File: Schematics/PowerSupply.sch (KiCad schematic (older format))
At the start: 0 parts

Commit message: Updated schematics
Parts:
- added C33: 10u, Capacitors_SMD:C_0603, symbol C
- added C34: 10n, Capacitors_SMD:C_0402, symbol C
- added C35: 1u, Capacitors_SMD:C_0402, symbol C
- added C36: 100n, Capacitors_SMD:C_0402, symbol C
- added C37: 10p, Capacitors_SMD:C_0402, symbol C
- added C38, C39: 47n, Capacitors_SMD:C_0603, symbol C
- added D1: LED, LEDs:LED-1206, symbol LED
- added L1: 3.2u, symbol INDUCTOR
- added R31: 220R, Resistors_SMD:R_0603, symbol R
- added R32: 41.2k, Resistors_SMD:R_0402, symbol R
- added R33: 2.4M, Resistors_SMD:R_0402, symbol R
- added R34: 1M, Resistors_SMD:R_0402, symbol R
- added U13: LT8612, rgb:28QFN, symbol LT8612
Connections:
- net labels added: BST, FB, GND, IntVcc, PG, Rt, SS, SW, Vin, Vsupply
- wire segments 0 -> 47

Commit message: Removed RF. Placed all LED drivers and passives and begun routing
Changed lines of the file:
@@
 $Descr A4 11693 8268
 encoding utf-8
-Sheet 17 16
+Sheet 16 16
 Title ""
 Date ""
@@
 	3600 2900 3600 3800
 $Comp
-L GND #PWR0134
+L GND #PWR0117
 U 1 1 54BACD64
 P 3900 3900
-F 0 "#PWR0134" H 3900 3650 60  0001 C CNN
+F 0 "#PWR0117" H 3900 3650 60  0001 C CNN
 F 1 "GND" H 3900 3750 60  0000 C CNN
 F 2 "" H 3900 3900 60  0000 C CNN
@@
 	6050 3150 6050 3400
 Wire Wire Line
-	6950 3400 6050 3400
+	6050 3400 6950 3400
 Wire Wire Line
 	6950 3300 6950 3450
@@
 Connection ~ 7600 2750
 $Comp
-L GND #PWR0135
+L GND #PWR0118
 U 1 1 54BAE2C1
 P 4850 3900
-F 0 "#PWR0135" H 4850 3650 60  0001 C CNN
+F 0 "#PWR0118" H 4850 3650 60  0001 C CNN
 F 1 "GND" H 4850 3750 60  0000 C CNN
 F 2 "" H 4850 3900 60  0000 C CNN
@@
 $EndComp
 $Comp
-L GND #PWR0136
+L GND #PWR0119
 U 1 1 54BAE2D9
 P 5150 3900
-F 0 "#PWR0136" H 5150 3650 60  0001 C CNN
+F 0 "#PWR0119" H 5150 3650 60  0001 C CNN
 F 1 "GND" H 5150 3750 60  0000 C CNN
 F 2 "" H 5150 3900 60  0000 C CNN
@@
 $EndComp
 $Comp
-L GND #PWR0137
+L GND #PWR0120
 U 1 1 54BAE2F1
 P 6950 4000
-F 0 "#PWR0137" H 6950 3750 60  0001 C CNN
+F 0 "#PWR0120" H 6950 3750 60  0001 C CNN
 F 1 "GND" H 6950 3850 60  0000 C CNN
 F 2 "" H 6950 4000 60  0000 C CNN
@@
 $EndComp
 $Comp
-L GND #PWR0138
+L GND #PWR0121
 U 1 1 54BAE309
 P 7800 4050
-F 0 "#PWR0138" H 7800 3800 60  0001 C CNN
+F 0 "#PWR0121" H 7800 3800 60  0001 C CNN
 F 1 "GND" H 7800 3900 60  0000 C CNN
 F 2 "" H 7800 4050 60  0000 C CNN

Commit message: Changed lots
Finalised the Inductor. Closes #5
Changed USB Connector. Closes #4
Added four switches for a simple interface. Closes #7
Added a power jack. Closes #3
Found RTC Oscillator. Closes #1.
Added part numbers to all major components. Closes #2
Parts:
- L1: footprint (none) -> rgb:SD43; Part (none) -> SD43-332ML
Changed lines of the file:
@@
 F 0 "L1" V 6450 2500 50  0000 C CNN
 F 1 "3.2u" V 6450 2850 50  0000 C CNN
-F 2 "" H 6500 2750 60  0001 C CNN
-F 3 "" H 6500 2750 60  0000 C CNN
+F 2 "rgb:SD43" H 6500 2750 60  0001 C CNN
+F 3 "http://www.coilcraft.com/pdfs/sd43.pdf" H 6500 2750 60  0001 C CNN
+F 4 "SD43-332ML" V 6500 2750 60  0001 C CNN "Part"
 	1    6500 2750
 	0    -1   -1   0
@@
 	3600 2900 3600 3800
 $Comp
-L GND #PWR118
+L GND #PWR0119
 U 1 1 54BACD64
 P 3900 3900
-F 0 "#PWR118" H 3900 3650 60  0001 C CNN
+F 0 "#PWR0119" H 3900 3650 60  0001 C CNN
 F 1 "GND" H 3900 3750 60  0000 C CNN
 F 2 "" H 3900 3900 60  0000 C CNN
@@
 Connection ~ 7600 2750
 $Comp
-L GND #PWR119
+L GND #PWR0120
 U 1 1 54BAE2C1
 P 4850 3900
-F 0 "#PWR119" H 4850 3650 60  0001 C CNN
+F 0 "#PWR0120" H 4850 3650 60  0001 C CNN
 F 1 "GND" H 4850 3750 60  0000 C CNN
 F 2 "" H 4850 3900 60  0000 C CNN
@@
 $EndComp
 $Comp
-L GND #PWR120
+L GND #PWR0121
 U 1 1 54BAE2D9
 P 5150 3900
-F 0 "#PWR120" H 5150 3650 60  0001 C CNN
+F 0 "#PWR0121" H 5150 3650 60  0001 C CNN
 F 1 "GND" H 5150 3750 60  0000 C CNN
 F 2 "" H 5150 3900 60  0000 C CNN
@@
 $EndComp
 $Comp
-L GND #PWR121
+L GND #PWR0122
 U 1 1 54BAE2F1
 P 6950 4000
-F 0 "#PWR121" H 6950 3750 60  0001 C CNN
+F 0 "#PWR0122" H 6950 3750 60  0001 C CNN
 F 1 "GND" H 6950 3850 60  0000 C CNN
 F 2 "" H 6950 4000 60  0000 C CNN
@@
 $EndComp
 $Comp
-L GND #PWR122
+L GND #PWR0123
 U 1 1 54BAE309
 P 7800 4050
-F 0 "#PWR122" H 7800 3800 60  0001 C CNN
+F 0 "#PWR0123" H 7800 3800 60  0001 C CNN
 F 1 "GND" H 7800 3900 60  0000 C CNN
 F 2 "" H 7800 4050 60  0000 C CNN

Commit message: Ammended a net. Done a lot of routing
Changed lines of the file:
@@
 U 1 1 54BABE93
 P 5950 2550
-F 0 "C36" V 5900 2350 50  0000 L CNN
+F 0 "C36" V 5800 2500 50  0000 L CNN
 F 1 "100n" V 5900 2700 50  0000 L CNN
 F 2 "Capacitors_SMD:C_0402" H 5988 2400 30  0001 C CNN

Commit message: Started Redesign.
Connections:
- wire segments 47 -> 48
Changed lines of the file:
@@
 $Descr A4 11693 8268
 encoding utf-8
-Sheet 16 16
+Sheet 3 3
 Title ""
 Date ""
@@
 	4100 2800 4400 2800
 Wire Wire Line
-	4100 2400 4100 2800
+	4100 2300 4100 2800
 Wire Wire Line
 	3600 2900 4400 2900
@@
 	4400 3200 4300 3200
 Wire Wire Line
-	4300 3200 4300 3250
+	4300 3200 4300 3350
 Wire Wire Line
 	4400 3100 4050 3100
 Wire Wire Line
-	4050 3100 4050 3300
+	4050 3100 4050 3350
 Wire Wire Line
 	4400 3000 3750 3000
 Wire Wire Line
-	3750 3000 3750 3300
-Wire Wire Line
-	3400 2850 3400 2550
+	3750 3000 3750 3350
+Wire Wire Line
+	3400 2550 3400 2900
 Connection ~ 3400 2550
 Wire Wire Line
 	3600 2900 3600 3800
 $Comp
-L GND #PWR0119
+L GND #PWR047
 U 1 1 54BACD64
 P 3900 3900
-F 0 "#PWR0119" H 3900 3650 60  0001 C CNN
+F 0 "#PWR047" H 3900 3650 60  0001 C CNN
 F 1 "GND" H 3900 3750 60  0000 C CNN
 F 2 "" H 3900 3900 60  0000 C CNN
@@
 $EndComp
 Wire Wire Line
-	3400 3250 3400 3800
+	3400 3200 3400 3800
 Wire Wire Line
 	3400 3800 4300 3800
 Wire Wire Line
-	4300 3800 4300 3750
-Wire Wire Line
-	4050 3700 4050 3800
+	4300 3800 4300 3650
+Wire Wire Line
+	4050 3650 4050 3800
 Connection ~ 4050 3800
 Wire Wire Line
-	3750 3700 3750 3800
+	3750 3650 3750 3800
 Connection ~ 3750 3800
 Connection ~ 3600 3800
@@
 Connection ~ 3900 3800
 Wire Wire Line
-	5600 2550 5750 2550
+	5600 2550 5800 2550
 Wire Wire Line
 	5600 2750 6200 2750
@@
 	6800 2750 8350 2750
 Wire Wire Line
-	7200 2850 7200 2750
+	7200 2750 7200 2900
 Connection ~ 7200 2750
 Wire Wire Line
-	6950 2800 6950 2750
+	6950 2750 6950 2900
 Connection ~ 6950 2750
 Wire Wire Line
@@
 	6050 3400 6950 3400
 Wire Wire Line
-	6950 3300 6950 3450
+	6950 3200 6950 3500
 Connection ~ 6950 3400
 Wire Wire Line
-	6950 3350 7200 3350
-Wire Wire Line
-	7200 3350 7200 3250
+	7200 3350 6950 3350
+Wire Wire Line
+	7200 3200 7200 3350
 Connection ~ 6950 3350
 Wire Wire Line
-	7950 2850 7950 2750
+	7950 2750 7950 2900
 Connection ~ 7950 2750
 Wire Wire Line
-	7600 2850 7600 2750
+	7600 2750 7600 2900
 Connection ~ 7600 2750
 $Comp
-L GND #PWR0120
+L GND #PWR048
 U 1 1 54BAE2C1
 P 4850 3900
-F 0 "#PWR0120" H 4850 3650 60  0001 C CNN
+F 0 "#PWR048" H 4850 3650 60  0001 C CNN
 F 1 "GND" H 4850 3750 60  0000 C CNN
 F 2 "" H 4850 3900 60  0000 C CNN
@@
 $EndComp
 $Comp
-L GND #PWR0121
+L GND #PWR049
 U 1 1 54BAE2D9
 P 5150 3900
-F 0 "#PWR0121" H 5150 3650 60  0001 C CNN
+F 0 "#PWR049" H 5150 3650 60  0001 C CNN
 F 1 "GND" H 5150 3750 60  0000 C CNN
 F 2 "" H 5150 3900 60  0000 C CNN
@@
 $EndComp
 $Comp
-L GND #PWR0122
+L GND #PWR050
 U 1 1 54BAE2F1
 P 6950 4000
-F 0 "#PWR0122" H 6950 3750 60  0001 C CNN
+F 0 "#PWR050" H 6950 3750 60  0001 C CNN
 F 1 "GND" H 6950 3850 60  0000 C CNN
 F 2 "" H 6950 4000 60  0000 C CNN
@@
 $EndComp
 $Comp
-L GND #PWR0123
+L GND #PWR051
 U 1 1 54BAE309
 P 7800 4050
-F 0 "#PWR0123" H 7800 3800 60  0001 C CNN
+F 0 "#PWR051" H 7800 3800 60  0001 C CNN
 F 1 "GND" H 7800 3900 60  0000 C CNN
 F 2 "" H 7800 4050 60  0000 C CNN
@@
 $EndComp
 Wire Wire Line
-	7600 3250 7600 4000
+	7600 3200 7600 4000
 Wire Wire Line
 	7600 4000 7950 4000
 Wire Wire Line
-	7950 4000 7950 3250
+	7950 4000 7950 3200
 Wire Wire Line
 	7800 4050 7800 4000
 Connection ~ 7800 4000
 Wire Wire Line
-	6950 3900 6950 4000
+	6950 3800 6950 4000
 Wire Wire Line
 	4850 3600 4850 3900
@@
 $EndComp
 Wire Wire Line
-	4100 1900 4100 1850
+	4100 1850 4100 2000
 Wire Wire Line
 	4100 1400 4100 1450
@@
 	6850 2950 6850 2750
 Connection ~ 6850 2750
+Wire Wire Line
+	6150 2550 6100 2550
 $EndSCHEMATC

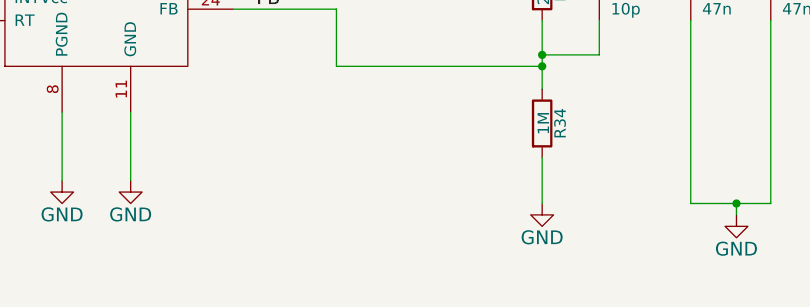
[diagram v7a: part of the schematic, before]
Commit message: Split design into two modules
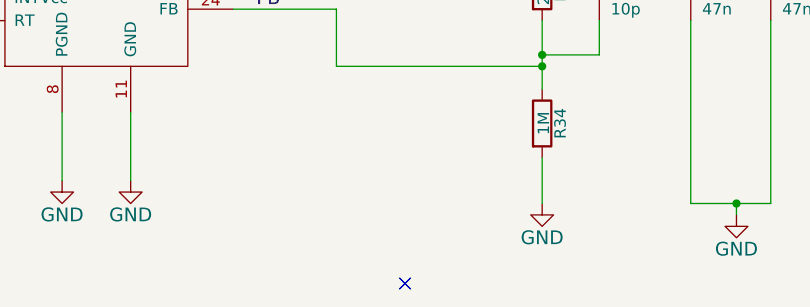
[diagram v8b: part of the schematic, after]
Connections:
- no-connect marks 0 -> 1
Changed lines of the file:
@@
 	3600 2900 3600 3800
 $Comp
-L GND #PWR047
+L GND #PWR046
 U 1 1 54BACD64
 P 3900 3900
-F 0 "#PWR047" H 3900 3650 60  0001 C CNN
+F 0 "#PWR046" H 3900 3650 60  0001 C CNN
 F 1 "GND" H 3900 3750 60  0000 C CNN
 F 2 "" H 3900 3900 60  0000 C CNN
@@
 Connection ~ 7600 2750
 $Comp
-L GND #PWR048
+L GND #PWR047
 U 1 1 54BAE2C1
 P 4850 3900
-F 0 "#PWR048" H 4850 3650 60  0001 C CNN
+F 0 "#PWR047" H 4850 3650 60  0001 C CNN
 F 1 "GND" H 4850 3750 60  0000 C CNN
 F 2 "" H 4850 3900 60  0000 C CNN
@@
 $EndComp
 $Comp
-L GND #PWR049
+L GND #PWR048
 U 1 1 54BAE2D9
 P 5150 3900
-F 0 "#PWR049" H 5150 3650 60  0001 C CNN
+F 0 "#PWR048" H 5150 3650 60  0001 C CNN
 F 1 "GND" H 5150 3750 60  0000 C CNN
 F 2 "" H 5150 3900 60  0000 C CNN
@@
 $EndComp
 $Comp
-L GND #PWR050
+L GND #PWR049
 U 1 1 54BAE2F1
 P 6950 4000
-F 0 "#PWR050" H 6950 3750 60  0001 C CNN
+F 0 "#PWR049" H 6950 3750 60  0001 C CNN
 F 1 "GND" H 6950 3850 60  0000 C CNN
 F 2 "" H 6950 4000 60  0000 C CNN
@@
 $EndComp
 $Comp
-L GND #PWR051
+L GND #PWR050
 U 1 1 54BAE309
 P 7800 4050
-F 0 "#PWR051" H 7800 3800 60  0001 C CNN
+F 0 "#PWR050" H 7800 3800 60  0001 C CNN
 F 1 "GND" H 7800 3900 60  0000 C CNN
 F 2 "" H 7800 4050 60  0000 C CNN
@@
 Wire Wire Line
 	6150 2550 6100 2550
+NoConn ~ 6350 4350
 $EndSCHEMATC
